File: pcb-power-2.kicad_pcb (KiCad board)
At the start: 2 copper layers, 53.6 x 53.7 mm, 18 parts, among them J1 Conn_01x07_Socket, J12 Conn_01x02_Socket, J2 Conn_01x02_Socket, J3 Conn_01x02_Socket, Q2 NMOS, Q4 PMOS, U1 LM1117DT-5.0, U2 IRF7303, U3 LM1117DT-5.0, U4 IRF7104

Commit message: finished pcb design
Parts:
- added J4: Conn_01x02_Socket, Connector_JST:JST_XH_B2B-XH-A_1x02_P2.50mm_Vertical, F.Cu at (138.0, 67.7)
- added J5: Conn_01x03_Socket, Connector_JST:JST_XH_B3B-XH-A_1x03_P2.50mm_Vertical, F.Cu at (136.8, 53.0)
- added R1: 10k, Resistor_THT:R_Axial_DIN0207_L6.3mm_D2.5mm_P10.16mm_Horizontal, B.Cu at (137.7, 49.5)
- added R2: 10k, Resistor_THT:R_Axial_DIN0207_L6.3mm_D2.5mm_P10.16mm_Horizontal, F.Cu at (128.0, 104.2)
- added R3: 10k, Resistor_THT:R_Axial_DIN0207_L6.3mm_D2.5mm_P10.16mm_Horizontal, F.Cu at (152.2, 62.4)
- J1: value Conn_01x07_Socket -> Conn_01x04_Socket; footprint Connector_PinSocket_2.54mm:PinSocket_1x07_P2.54mm_Vertical -> Connector_JST:JST_XH_B4B-XH-A_1x04_P2.50mm_Vertical
- J12, R5: moved to B.Cu
- moved R6 40.7 mm to (131.0, 60.1)
- moved R9 40.2 mm to (151.9, 76.8)
- moved R5 36.8 mm to (129.0, 66.1)
- moved C1 36.6 mm to (147.8, 68.2), turned to 90 degrees
- moved Q4 36.1 mm to (135.5, 77.0)
- moved R7 35.0 mm to (131.5, 65.2), turned to -90 degrees
- moved U4 34.7 mm to (140.5, 84.6), turned to 90 degrees
- moved U1 33.7 mm to (148.0, 85.8), turned to 90 degrees
- moved Q2 33.3 mm to (133.5, 84.0), turned to 0 degrees
- moved J3 32.0 mm to (145.2, 100.5), turned to 90 degrees
- moved J12 29.8 mm to (130.0, 68.0), turned to -90 degrees
- moved J1 20.2 mm to (135.5, 60.8)
- moved R8 19.1 mm to (129.0, 85.1), turned to 90 degrees
- moved R10 15.1 mm to (139.3, 90.5)
- moved U3 14.9 mm to (148.0, 74.0), turned to 90 degrees
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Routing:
- net VCC main: track 278.1 -> 46.8 mm, vias 1 -> 0
- net GND: track 257.8 -> 159.7 mm, vias 1 -> 0
- net PYRO 1: track 4.26 -> 93.9 mm
- net PYRO 2: track 4.26 -> 82.9 mm, vias 0 -> 2
- net signal: track 115.7 -> 42.7 mm
- net PROBE sec: track 77.2 -> 30.1 mm
- net Net-(U3-VI): track 50.1 -> 5.84 mm
- net PROBE main: track 18.4 -> 51.2 mm
- net MODE: track 53.2 -> 23.8 mm
- net Net-(U1-VI): track 30.3 -> 6.35 mm
- net +3.3V: track 55.0 -> 34.3 mm
- net Net-(J3-Pin_1): track 12.1 -> 16.4 mm
- net Net-(J2-Pin_1): track 11.7 -> 7.57 mm
- net VCC secondary: track 32.4 -> 31.0 mm, vias 0 -> 1
- net Net-(Q4-D): track 22.4 -> 21.5 mm
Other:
- board size 53.6 x 53.7 mm -> 30 x 58 mm

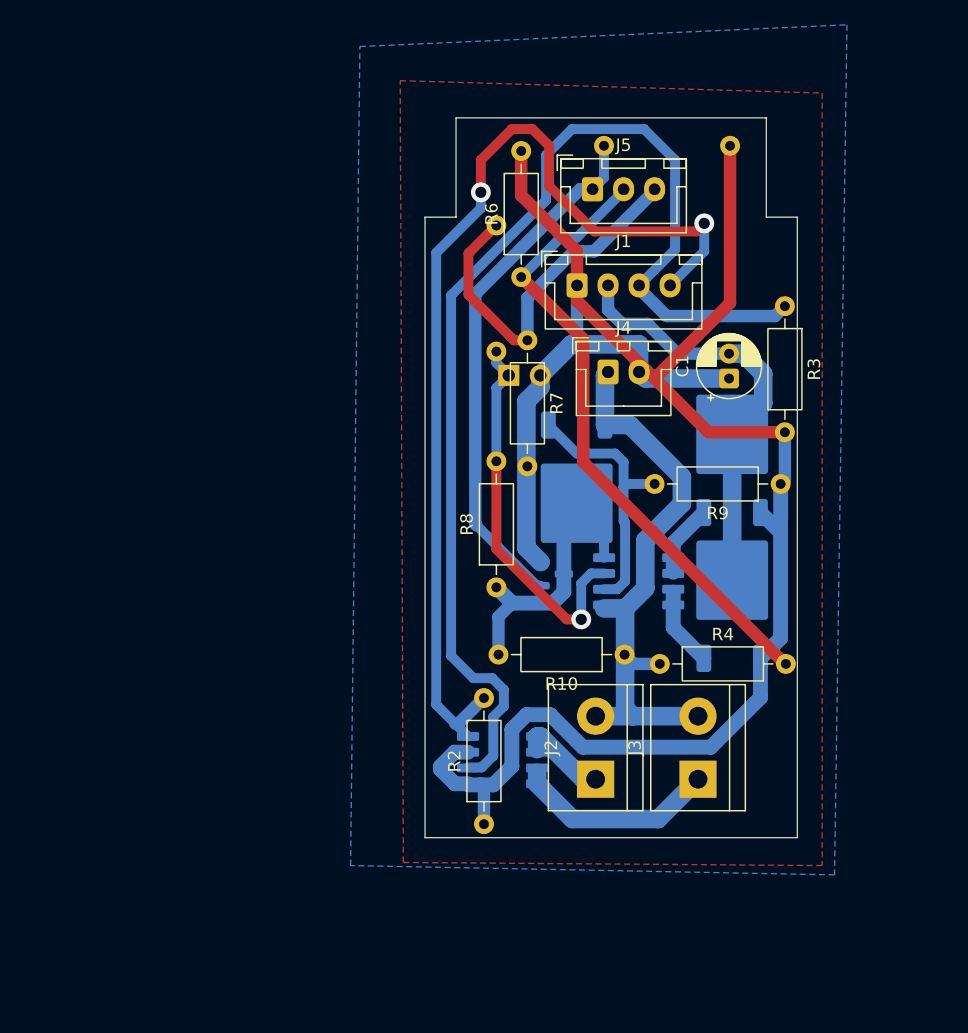
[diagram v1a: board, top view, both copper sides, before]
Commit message: corrected P-mosfet connection
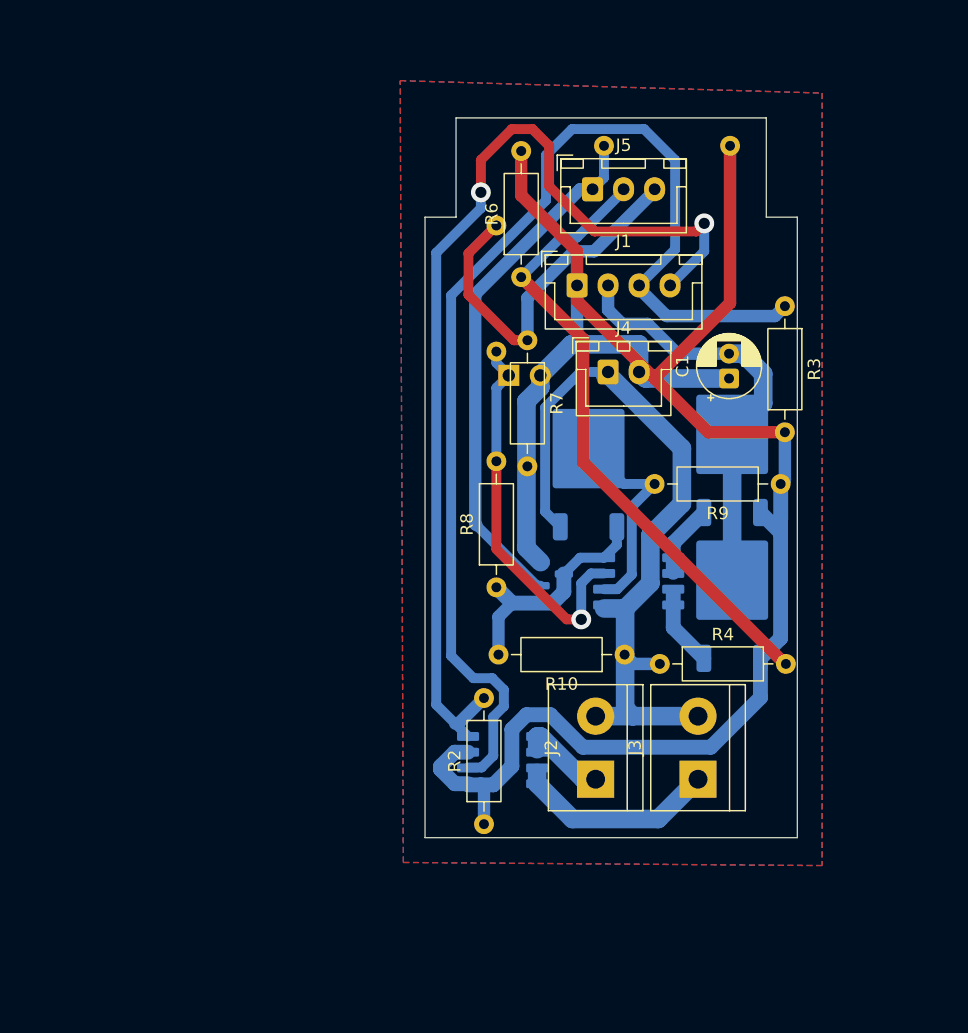
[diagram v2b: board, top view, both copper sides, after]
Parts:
- moved Q4 2.11 mm to (136.4, 75.2), turned to 90 degrees
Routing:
- net VCC main: track 46.8 -> 62.2 mm
- net MODE: track 23.8 -> 19.1 mm
- net Net-(Q4-D): track 21.5 -> 17.3 mm

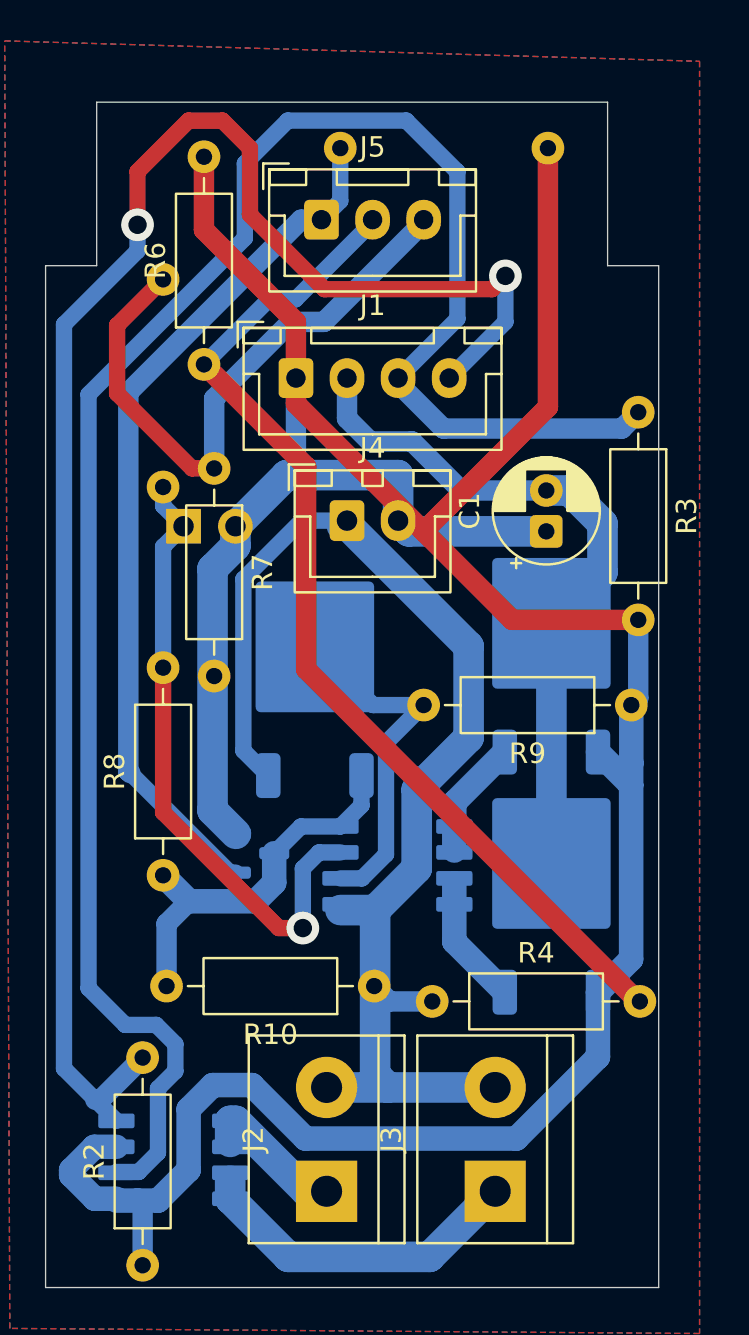
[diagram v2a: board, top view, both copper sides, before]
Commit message: added silkscreen markings
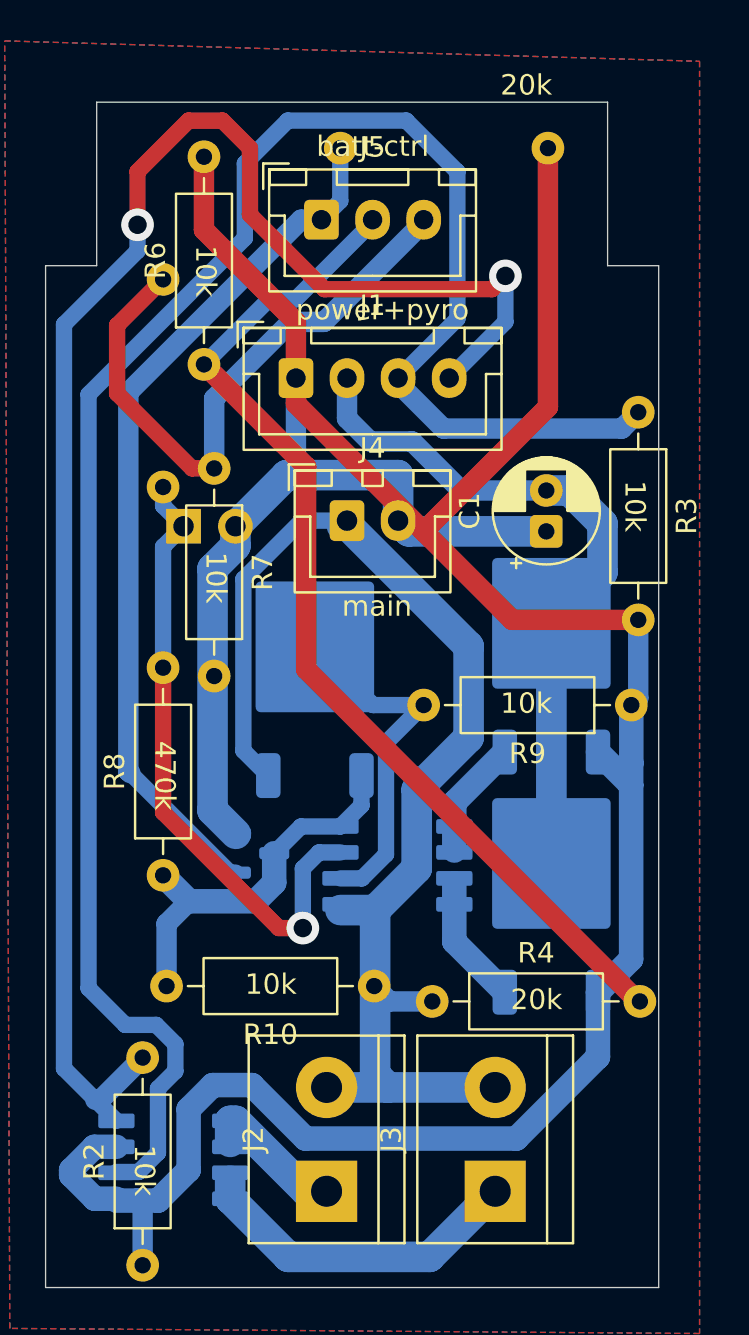
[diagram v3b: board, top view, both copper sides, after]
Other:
- board text added: "10k"
- board text added: "20k"
- board text added: "3V3"
- board text added: "470k"
- board text added: "P-mos"
- board text added: "batt-ctrl"
- board text added: "main"
- board text added: "power+pyro"
- board text added: "sec"
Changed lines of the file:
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@@
 		(tenting front back)
 		(pcbplotparams
-			(layerselection 0x00000000_00000000_55555555_55555551)
+			(layerselection 0x00000000_00000000_55555555_55555554)
 			(plot_on_all_layers_selection 0x00000000_00000000_00000000_00000000)
 			(disableapertmacros no)
@@
 			(subtractmaskfromsilk no)
 			(outputformat 5)
-			(mirror yes)
+			(mirror no)
 			(drillshape 0)
 			(scaleselection 1)
@@
 		(tags "Through hole socket strip THT 1x02 2.54mm single row")
 		(property "Reference" "J12"
-			(at 0 2.77 90)
+			(at 2 2.5 90)
 			(layer "B.SilkS")
 			(effects
@@
 	)
 	(gr_circle
-		(center 129 75)
-		(end 127.25 77.25)
-		(stroke
-			(width 0.1)
-			(type default)
-		)
-		(fill no)
-		(layer "Dwgs.User")
-	)
-	(gr_circle
 		(center 130.899561 49.75)
 		(end 129.149561 52)
@@
 		(layer "Dwgs.User")
 	)
-	(gr_circle
-		(center 151.75 76.75)
-		(end 150 79)
-		(stroke
-			(width 0.1)
-			(type default)
-		)
-		(fill no)
-		(layer "Dwgs.User")
-	)
-	(gr_circle
-		(center 131.5 65.5)
-		(end 129.75 67.75)
-		(stroke
-			(width 0.1)
-			(type default)
-		)
-		(fill no)
-		(layer "Dwgs.User")
-	)
 	(gr_line
 		(start 153.25 55.25)
@@
 		(layer "Edge.Cuts")
 	)
+	(gr_text "10k\n"
+		(at 127.5 98.25 270)
+		(layer "F.SilkS")
+		(effects
+			(font
+				(size 1 1)
+				(thickness 0.1)
+			)
+			(justify left bottom)
+		)
+	)
+	(gr_text "batt-ctrl"
+		(at 136.5 50 0)
+		(layer "F.SilkS")
+		(effects
+			(font
+				(size 1 1)
+				(thickness 0.1)
+			)
+			(justify left bottom)
+		)
+	)
+	(gr_text "10k\n"
+		(at 145.5 77.25 0)
+		(layer "F.SilkS")
+		(effects
+			(font
+				(size 1 1)
+				(thickness 0.1)
+			)
+			(justify left bottom)
+		)
+	)
+	(gr_text "10k\n"
+		(at 130.5 54.25 270)
+		(layer "F.SilkS")
+		(effects
+			(font
+				(size 1 1)
+				(thickness 0.1)
+			)
+			(justify left bottom)
+		)
+	)
+	(gr_text "20k\n"
+		(at 146 91.75 0)
+		(layer "F.SilkS")
+		(effects
+			(font
+				(size 1 1)
+				(thickness 0.1)
+			)
+			(justify left bottom)
+		)
+	)
+	(gr_text "10k\n"
+		(at 151.5 65.75 270)
+		(layer "F.SilkS")
+		(effects
+			(font
+				(size 1 1)
+				(thickness 0.1)
+			)
+			(justify left bottom)
+		)
+	)
+	(gr_text "power+pyro"
+		(at 135.5 58 0)
+		(layer "F.SilkS")
+		(effects
+			(font
+				(size 1 1)
+				(thickness 0.1)
+			)
+			(justify left bottom)
+		)
+	)
+	(gr_text "20k\n"
+		(at 145.5 47 0)
+		(layer "F.SilkS")
+		(effects
+			(font
+				(size 1 1)
+				(thickness 0.1)
+			)
+			(justify left bottom)
+		)
+	)
+	(gr_text "10k\n"
+		(at 131 69.25 270)
+		(layer "F.SilkS")
+		(effects
+			(font
+				(size 1 1)
+				(thickness 0.1)
+			)
+			(justify left bottom)
+		)
+	)
+	(gr_text "470k"
+		(at 128.5 78.5 270)
+		(layer "F.SilkS")
+		(effects
+			(font
+				(size 1 1)
+				(thickness 0.1)
+			)
+			(justify left bottom)
+		)
+	)
+	(gr_text "10k\n"
+		(at 133 91 0)
+		(layer "F.SilkS")
+		(effects
+			(font
+				(size 1 1)
+				(thickness 0.1)
+			)
+			(justify left bottom)
+		)
+	)
+	(gr_text "main"
+		(at 137.75 72.5 0)
+		(layer "F.SilkS")
+		(effects
+			(font
+				(size 1 1)
+				(thickness 0.1)
+			)
+			(justify left bottom)
+		)
+	)
+	(gr_text "sec"
+		(at 127.75 68.5 0)
+		(layer "B.SilkS")
+		(effects
+			(font
+				(size 1 1)
+				(thickness 0.1)
+			)
+			(justify left bottom mirror)
+		)
+	)
+	(gr_text "3V3"
+		(at 149.25 77.75 0)
+		(layer "B.SilkS")
+		(effects
+			(font
+				(size 1 1)
+				(thickness 0.1)
+			)
+			(justify left bottom mirror)
+		)
+	)
+	(gr_text "3V3"
+		(at 149.25 89.25 0)
+		(layer "B.SilkS")
+		(effects
+			(font
+				(size 1 1)
+				(thickness 0.1)
+			)
+			(justify left bottom mirror)
+		)
+	)
+	(gr_text "P-mos"
+		(at 139 78.75 0)
+		(layer "B.SilkS")
+		(effects
+			(font
+				(size 1 1)
+				(thickness 0.1)
+			)
+			(justify left bottom mirror)
+		)
+	)
+	(gr_text "10k"
+		(at 144.25 50 0)
+		(layer "B.SilkS")
+		(effects
+			(font
+				(size 1 1)
+				(thickness 0.1)
+			)
+			(justify left bottom mirror)
+		)
+	)
+	(gr_text "10k"
+		(at 128.75 62.25 270)
+		(layer "B.SilkS")
+		(effects
+			(font
+				(size 1 1)
+				(thickness 0.1)
+			)
+			(justify left bottom mirror)
+		)
+	)
 	(segment

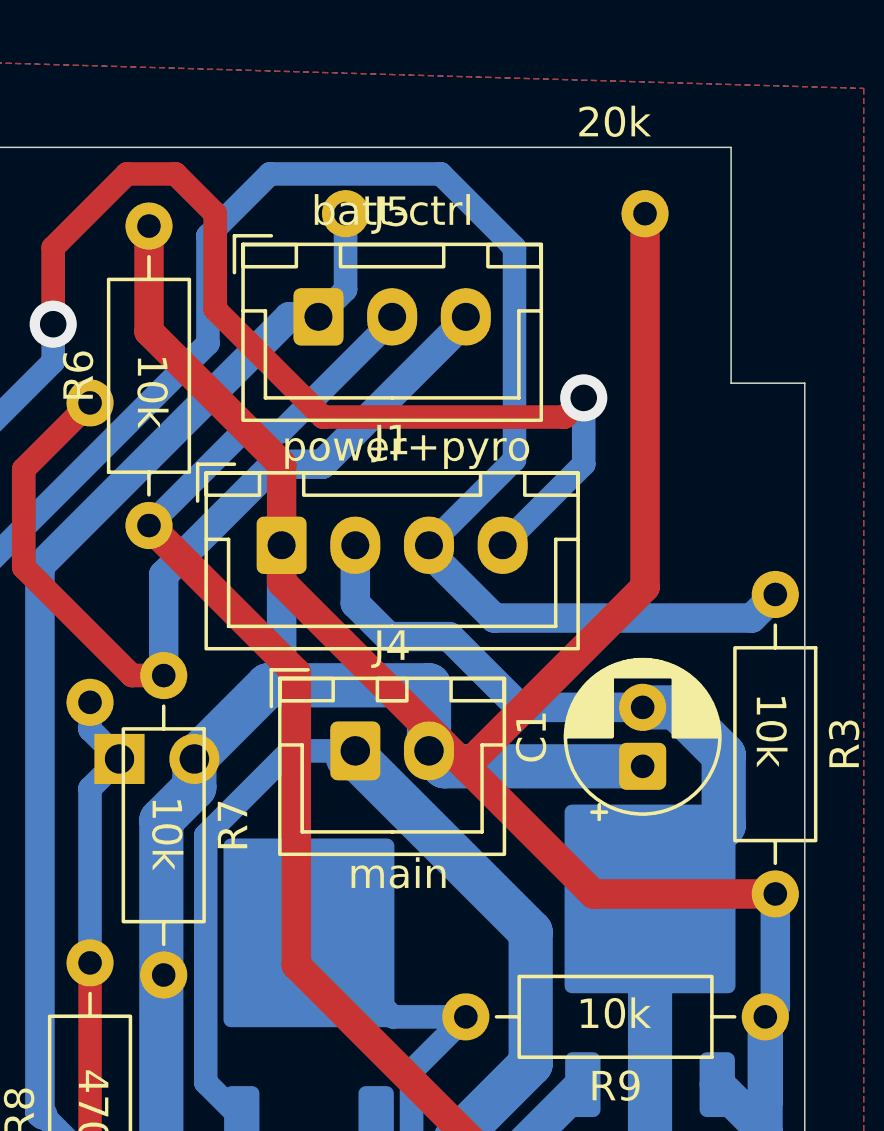
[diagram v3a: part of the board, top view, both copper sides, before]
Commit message: Changed JST footprints
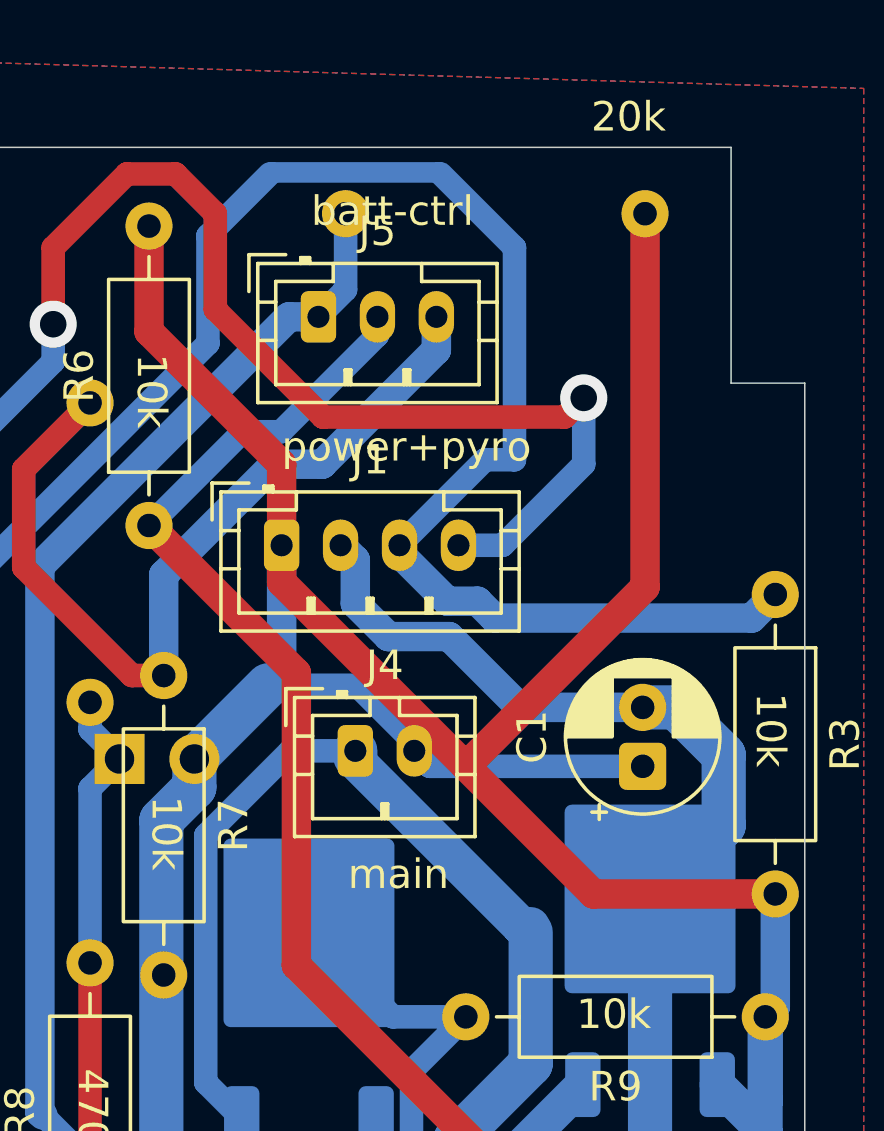
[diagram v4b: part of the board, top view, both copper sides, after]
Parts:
- J1: footprint Connector_JST:JST_XH_B4B-XH-A_1x04_P2.50mm_Vertical -> Connector_JST:JST_PH_B4B-PH-K_1x04_P2.00mm_Vertical
- J4: footprint Connector_JST:JST_XH_B2B-XH-A_1x02_P2.50mm_Vertical -> Connector_JST:JST_PH_B2B-PH-K_1x02_P2.00mm_Vertical
- J5: footprint Connector_JST:JST_XH_B3B-XH-A_1x03_P2.50mm_Vertical -> Connector_JST:JST_PH_B3B-PH-K_1x03_P2.00mm_Vertical
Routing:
- net PYRO 1: track 93.9 -> 95.9 mm
- net PYRO 2: track 82.9 -> 84.4 mm
- net GND: track 159.7 -> 158.6 mm
